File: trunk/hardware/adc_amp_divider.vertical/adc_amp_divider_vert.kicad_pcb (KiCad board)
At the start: 2 copper layers, 44 x 70 mm, 84 parts, among them M200 CONN_1, M201 CONN_1, M202 CONN_1, P201 CONN_10X2, P202 CONN_3, P203 CONN_2, P204 CONN_1, P205 CONN_1, P207 CONN_2, P208 CONN_6, P209 CONN_1, U201 LMV324IDR, U202 LMV324IDR

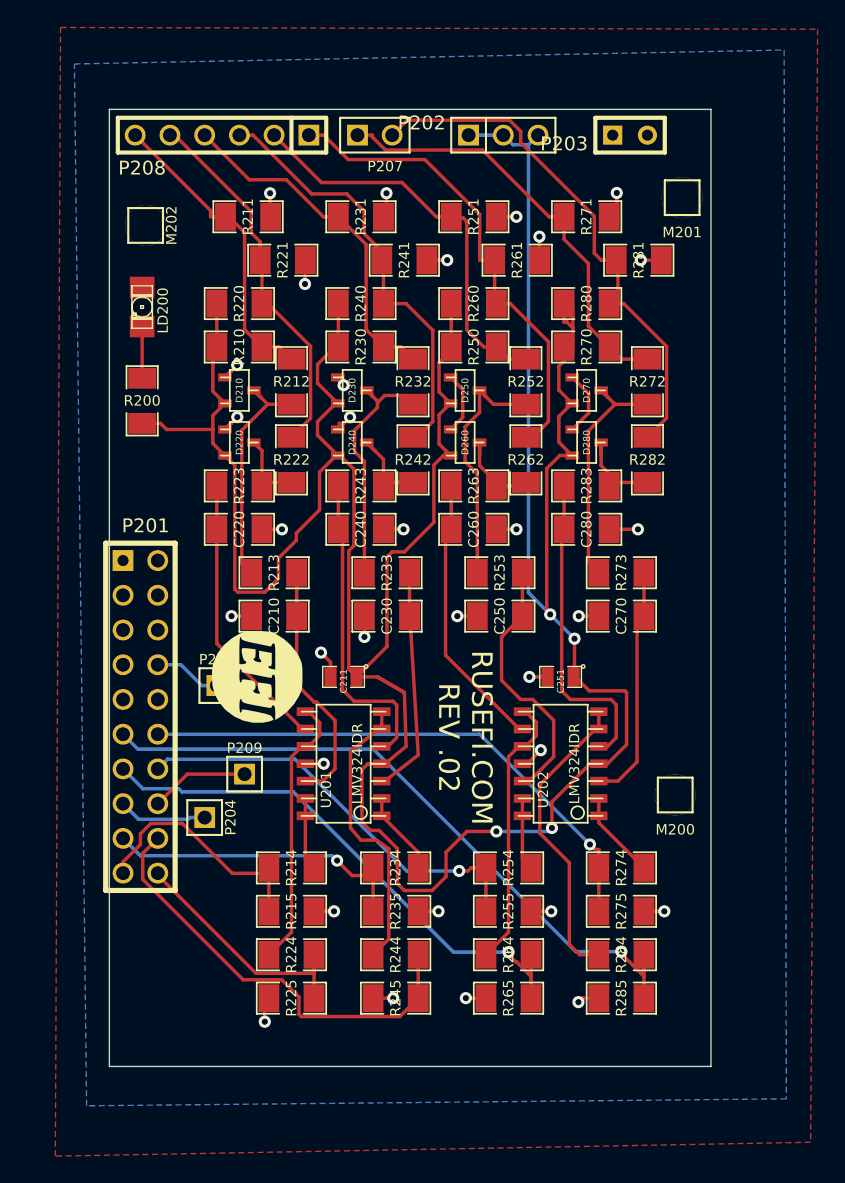
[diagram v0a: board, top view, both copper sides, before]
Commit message: design fixes by reducing some sizes to 0805
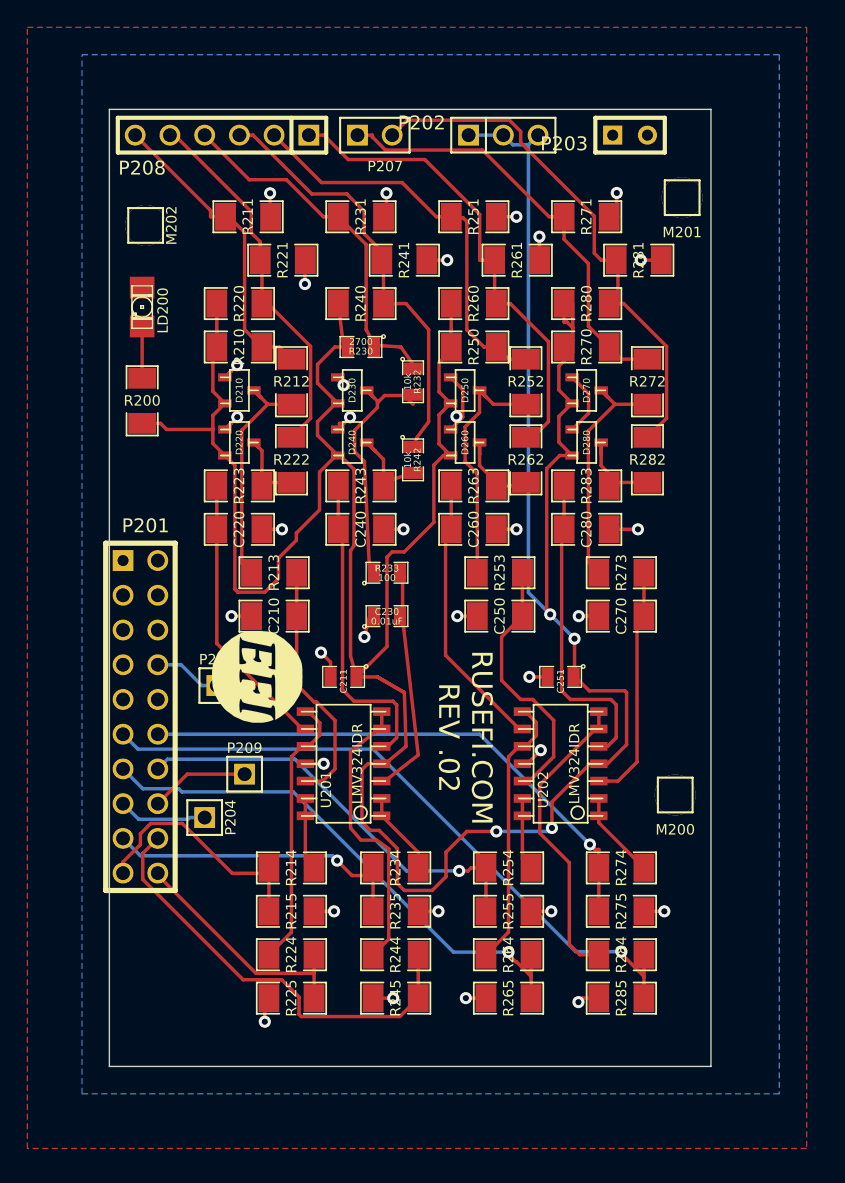
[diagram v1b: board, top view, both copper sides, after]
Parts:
- C230, R230, R232, R233, R242: footprint SM1206 -> SM0805
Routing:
- net GND: track 59.3 -> 59.7 mm, vias 32 -> 33
